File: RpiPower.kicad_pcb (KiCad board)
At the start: 2 copper layers, 42 x 64 mm, 17 parts, among them P1 header_pin, P2 Rpi_HDR-40, P3 header_pin, P4 header_pin, P5 header_pin, Q1 2N7002, Q2 2N7002, SW1 SW_PUSH, SW2 SW_PUSH

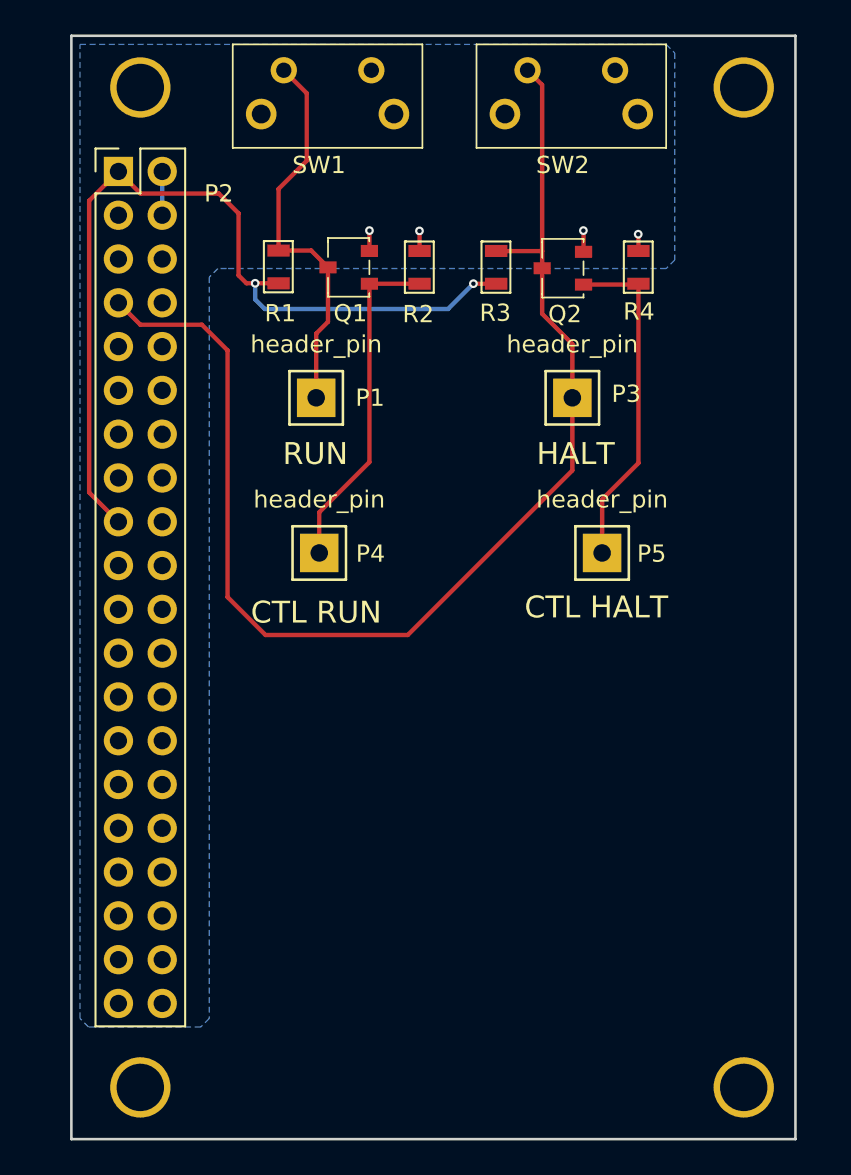
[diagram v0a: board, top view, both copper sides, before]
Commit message: changed from Raspberry pi 40-pin header to single pin headers to make the pcb smaller (cut size in half so half the cost)
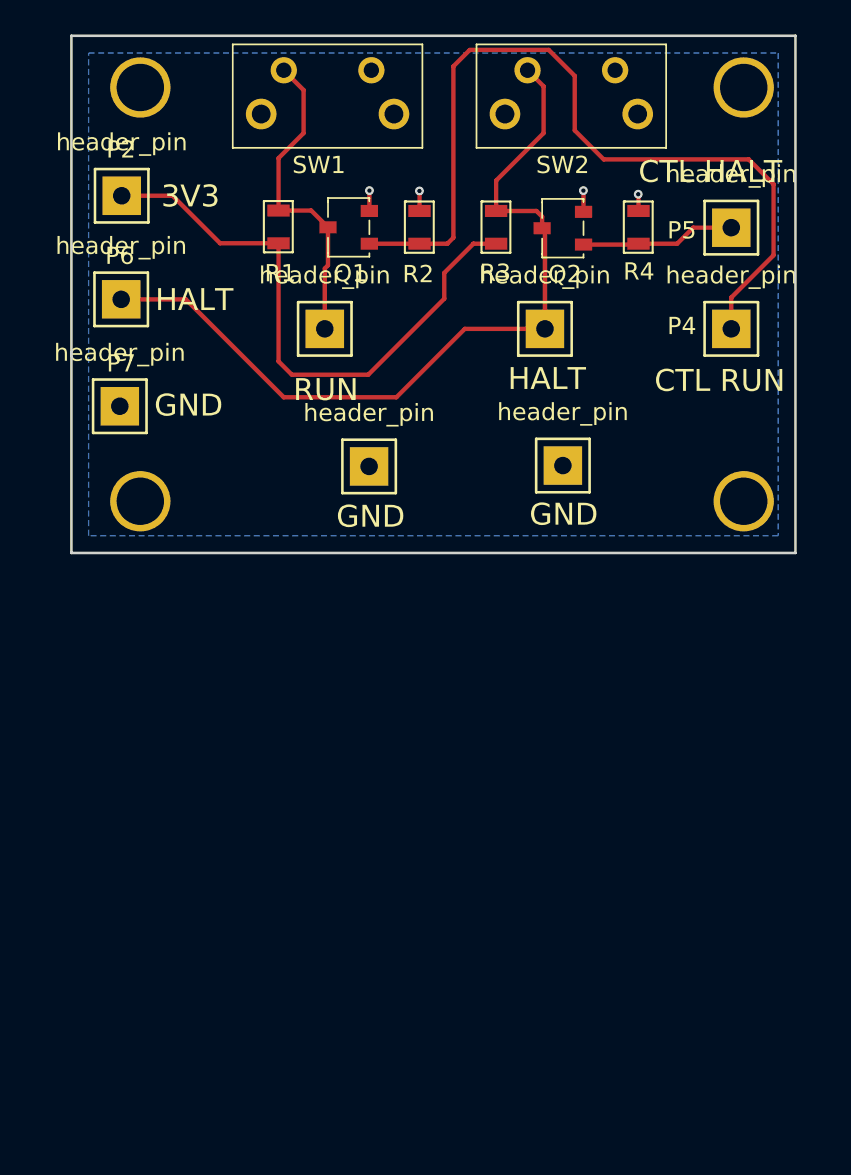
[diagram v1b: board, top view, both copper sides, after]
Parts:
- added P6: header_pin, footprints_on_Cdrive:Hdr_Pin, F.Cu at (118.9, 83.3)
- added P7: header_pin, footprints_on_Cdrive:Hdr_Pin, F.Cu at (118.8, 89.5)
- added P8: header_pin, footprints_on_Cdrive:Hdr_Pin, F.Cu at (133.3, 93.0)
- added P9: header_pin, footprints_on_Cdrive:Hdr_Pin, F.Cu at (144.5, 92.9)
- P2: value Rpi_HDR-40 -> header_pin; footprint footprints_on_Cdrive:header_2x20 -> footprints_on_Cdrive:Hdr_Pin
- moved MH2 34.0 mm to (120.0, 95.0)
- moved MH4 34.0 mm to (155.0, 95.0)
- moved P4 27.2 mm to (154.3, 85.0)
- moved P2 22.7 mm to (118.9, 77.3)
- moved P5 20.3 mm to (154.3, 79.1)
- moved P3 4.30 mm to (143.5, 85.0)
- moved P1 4.03 mm to (130.7, 85.0)
- moved Q1 2.32 mm to (130.9, 79.1)
- moved R2 2.32 mm to (136.2, 79.1)
- moved R3 2.32 mm to (140.6, 79.1)
- moved R4 2.32 mm to (148.9, 79.1)
- moved Q2 2.32 mm to (143.3, 79.2)
- moved R1 2.32 mm to (128.0, 79.1)
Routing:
- net /CTL_RUN: track 19.7 -> 48.4 mm
- net /HALT: track 73.6 -> 47.7 mm
- net /3V3: track 51.6 -> 34.1 mm, vias 2 -> 0
- net /CTL_HALT: track 19.7 -> 8.98 mm
- net /RUN: track 22.8 -> 18.5 mm
- net /5V: track 2.54 -> 0.00 mm
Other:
- board size 42 x 64 mm -> 42 x 30 mm
- board text added: "3V3"
- board text added: "GND"
